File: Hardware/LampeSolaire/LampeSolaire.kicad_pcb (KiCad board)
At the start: 2 copper layers, 85 x 100 mm, 126 parts, among them K1 RELAIS_DPDT, P1 1V8, P2 3V5, P3 3V5, T1 SI2333, T2 FDN337, T3 FDN337, T4 FDN337, T5 FDN337, U1 MCP73832, U2 MCP121, U3 NCP114ASN330T1G, U4 3V3 to 5V, U5 RF_RECEIVER, U6 PIC16F1827, U7 MCP6001R, U8 74LV00, X1 ICSP, X13 STOCK, X14 STOCK, X15 STOCK, X17 STOCK_1, X18 SOLAR_CELL, X2 PHOTO_RESISTOR, X3 WATER_SENSOR, X4 WATER_SENSOR, X5 LAMP, X6 STOCK_1, X8 BUZZER

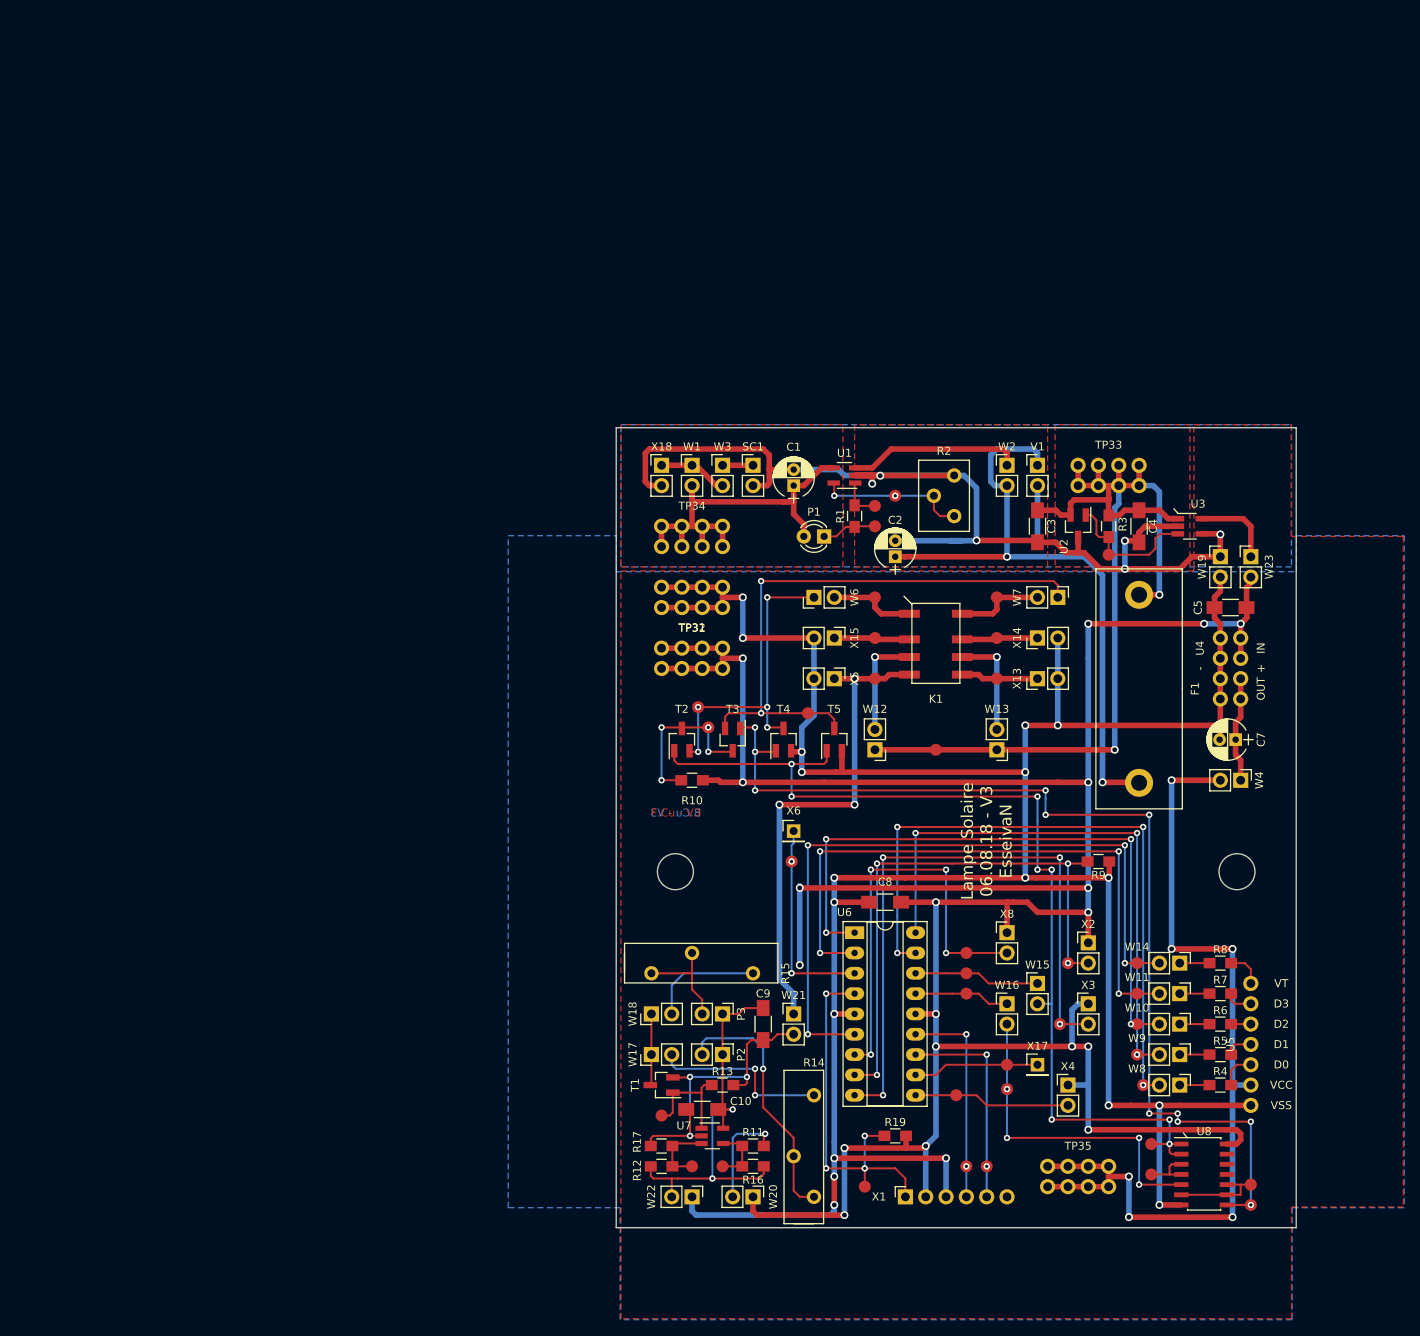
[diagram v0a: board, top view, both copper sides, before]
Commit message: Version 4
Nouveau PCB, modifications diverses au schéma
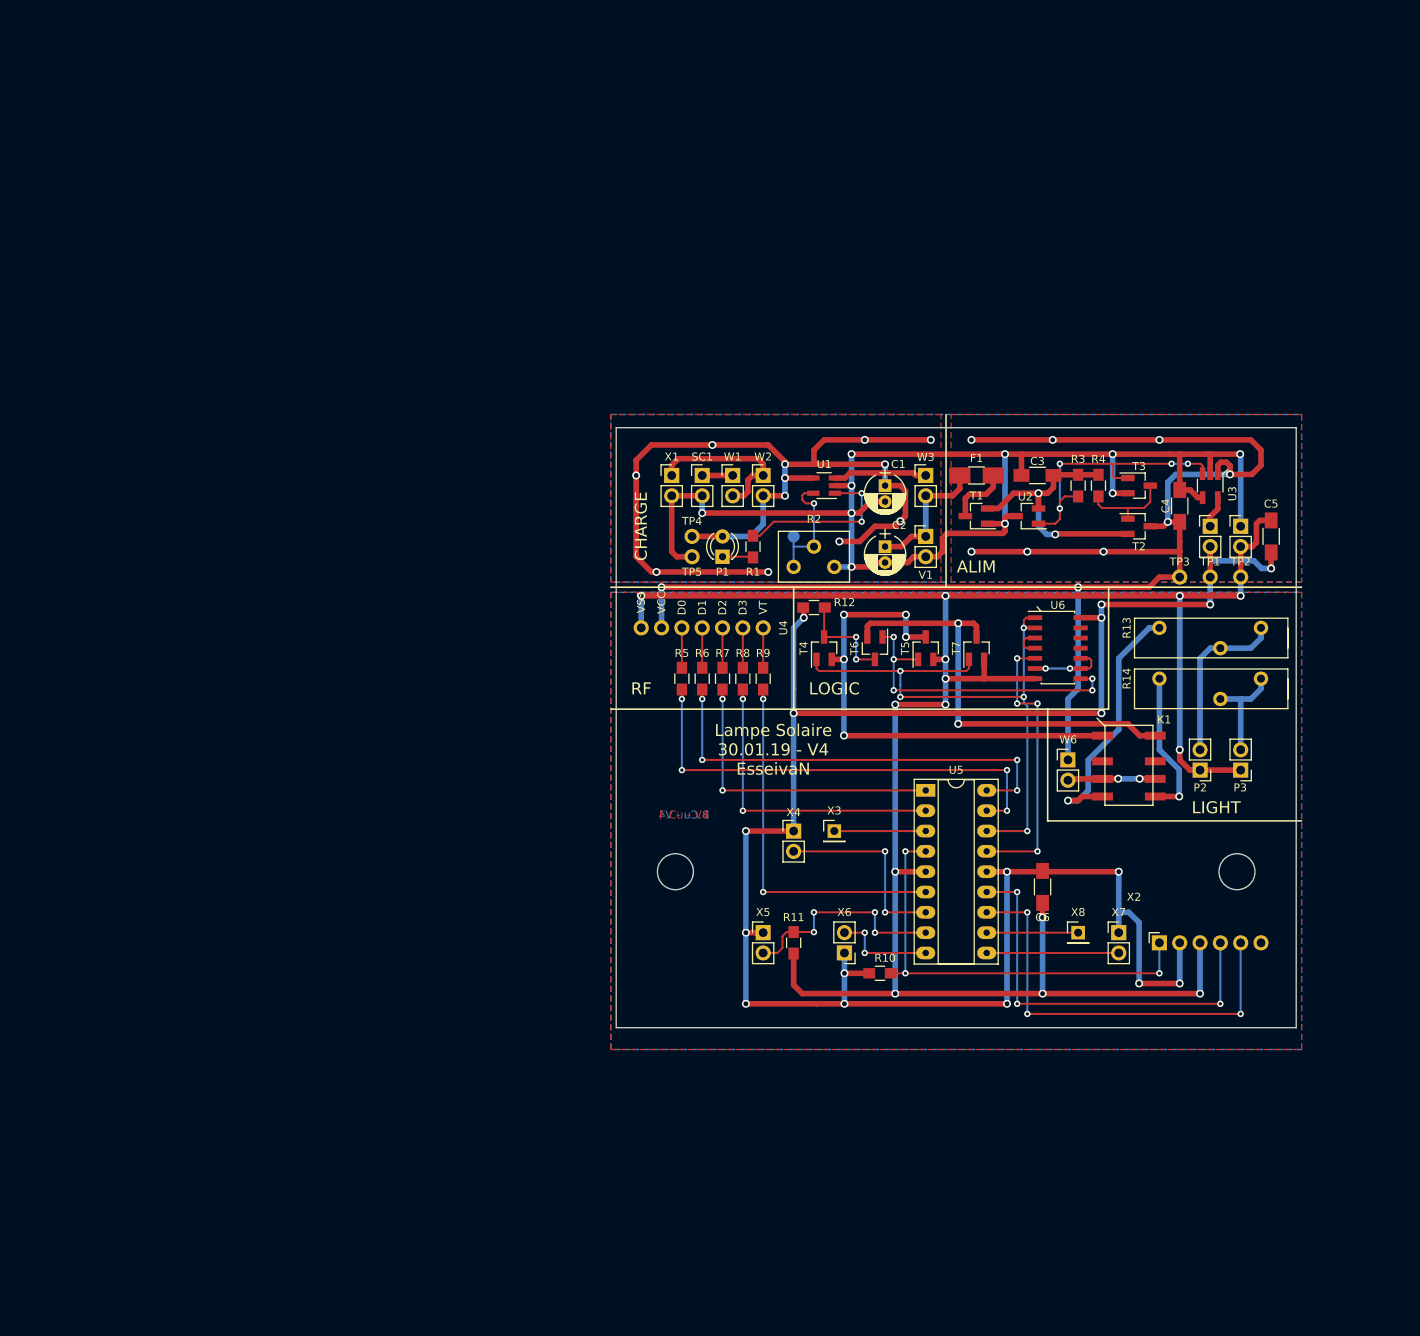
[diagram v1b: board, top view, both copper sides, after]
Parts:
- removed C10, C8, C9: 100nF, Capacitors_SMD:C_1206_HandSoldering
- removed C7: 4.7uF, MyLib:CP_Radial_D5.0mm_P2.00mm
- removed R15: 10, MyLib:Potentiometer_Trimmer_Bourns_3006P
- removed R16: 150k, MyLib:R_0805_HandSoldering
- removed R17: 100k, MyLib:R_0805_HandSoldering
- removed R19: 4k7, MyLib:R_0805_HandSoldering
- removed TP11, TP12, TP14, TP15, TP17, TP18, TP19, TP20, TP21, TP22, TP23, TP24, TP25, TP26, TP27, TP28, TP29, TP30, TP36, TP38, TP39, TP40, TP41, TP42, TP43, TP44, TP45, TP49, TP50, TP51, TP7, TP9: TestPoint, MyLib:Measurement_Point_Round-SMD-Pad_Small
- removed TP31, TP32, TP33, TP34, TP35: TestPoint_8, MyLib:Measurement_Point_Round-TH_Small_x8
- removed U7: MCP6001R, MyLib:SOT-23-5_HandSoldering
- removed U8: 74LV00, MyLib:SOIC-14
- removed W10, W11, W12, W13, W14, W15, W16, W17, W18, W19, W20, W21, W22, W23, W7, W8, W9: TEST_2P, MyLib:Pin_Header_Straight_1x02_Pitch2.54mm
- removed X13, X14, X15: STOCK, MyLib:Pin_Header_Straight_1x02_Pitch2.54mm
- removed X17: STOCK_1, MyLib:Pin_Header_Straight_1x01_Pitch2.54mm
- removed X18: SOLAR_CELL, MyLib:Pin_Header_Straight_1x02_Pitch2.54mm
- added C6: 100nF, Capacitors_SMD:C_1206_HandSoldering, F.Cu at (110.8, 101.9)
- added T6: FDN337, MyLib:SOT-23_Handsoldering, F.Cu at (89.8, 72.1)
- added T7: FDN337, MyLib:SOT-23_Handsoldering, F.Cu at (102.5, 72.1)
- added W5: TEST_2P, MyLib:Pin_Header_Straight_1x02_Pitch2.54mm, F.Cu at (131.8, 58.1)
- added X7: WATER_SENSOR, MyLib:Pin_Header_Straight_1x02_Pitch2.54mm, F.Cu at (120.3, 108.9)
- F1: footprint MyLib:FuseHolder_Schurter -> Fuse_Holders_and_Fuses:Fuse_SMD1206_HandSoldering
- R10: value 22 -> 4k7
- R11: value 110k -> 1M
- R12: value 100k -> 22
- R13: value 100k -> 10; footprint MyLib:R_0805_HandSoldering -> MyLib:Potentiometer_Trimmer_Bourns_3006P
- R4: value 4k7 -> 100k
- R5, R6, R7, R8: value 4k7 -> 1k
- R9: value 1M -> 4k7
- T2: value FDN337 -> SI2333
- TP1, TP2, TP3, TP4, TP5: value TestPoint -> TestPoint_8; footprint MyLib:Measurement_Point_Round-SMD-Pad_Small -> MyLib:Measurement_Point_Round-TH_Small
- TP6: moved to B.Cu
- U4: value 3V3 to 5V -> RF_RECEIVER; footprint MyLib:DC_DC -> MyLib:RF_RECEIVER
- U5: value RF_RECEIVER -> PIC16F1827; footprint MyLib:RF_RECEIVER -> MyLib:DIP-18
- U6: value PIC16F1827 -> 74xx00; footprint MyLib:DIP-18 -> MyLib:SOIC-14
- X1: value ICSP -> SOLAR_CELL; footprint MyLib:Pin_Header_Angled_1x06_Pitch2.54mm_reverse_invis -> MyLib:Pin_Header_Straight_1x02_Pitch2.54mm
- X2: value PHOTO_RESISTOR -> ICSP; footprint MyLib:Pin_Header_Straight_1x02_Pitch2.54mm -> MyLib:Pin_Header_Angled_1x06_Pitch2.54mm_reverse_invis
- X3: value WATER_SENSOR -> STOCK_1; footprint MyLib:Pin_Header_Straight_1x02_Pitch2.54mm -> MyLib:Pin_Header_Straight_1x01_Pitch2.54mm
- X4: value WATER_SENSOR -> BUZZER
- X5: value LAMP -> PHOTO_RESISTOR
- X6: value STOCK_1 -> WATER_SENSOR; footprint MyLib:Pin_Header_Straight_1x01_Pitch2.54mm -> MyLib:Pin_Header_Straight_1x02_Pitch2.54mm
- X8: value BUZZER -> STOCK_1; footprint MyLib:Pin_Header_Straight_1x02_Pitch2.54mm -> MyLib:Pin_Header_Straight_1x01_Pitch2.54mm
- moved X1 93.6 mm to (64.4, 51.7), turned to 0 degrees
- moved R5 82.1 mm to (65.7, 75.9), turned to 90 degrees
- moved T1 81.3 mm to (102.5, 55.5)
- moved R13 79.0 mm to (125.4, 69.5), turned to 180 degrees
- moved R6 77.8 mm to (68.2, 75.9), turned to 90 degrees
- moved R4 76.5 mm to (117.8, 51.7), turned to 90 degrees
- moved R7 73.6 mm to (70.8, 75.9), turned to 90 degrees
- moved P3 73.3 mm to (135.6, 86.0), turned to 180 degrees
- moved P2 71.2 mm to (130.5, 86.0), turned to 180 degrees
- moved R12 70.0 mm to (82.2, 67.0)
- moved R8 69.5 mm to (73.3, 75.9), turned to 90 degrees
- moved R14 67.6 mm to (125.4, 75.9), turned to 180 degrees
- moved U4 66.2 mm to (68.2, 69.5), turned to 0 degrees
- moved T2 63.1 mm to (122.9, 56.8), turned to 0 degrees
- moved T3 59.9 mm to (122.9, 51.7), turned to 0 degrees
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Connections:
- C3 pad 1: VBAT -> /VBAT_0
- F1 pad 1: VBAT -> Net-(F1-Pad1)
- K1 pad 4: LAMP -> Net-(K1-Pad4)
- K1 pad 6: Net-(K1-Pad6) -> Net-(K1-Pad3)
- P2 pad 1: Net-(C10-Pad2) -> GND
- P3 pad 1: Net-(C10-Pad2) -> GND
- R10 pad 1: Net-(R10-Pad1) -> /VPP
- R11 pad 1: /1V9 -> GND
- R12 pad 2: Net-(C10-Pad1) -> VCC
- R13 pad 1: Net-(R13-Pad1) -> Net-(K1-Pad4)
- R13 pad 2: Net-(C10-Pad1) -> Net-(P2-Pad2)
- R14 pad 1: Net-(R14-Pad1) -> Net-(K1-Pad5)
- R14 pad 2: Net-(P2-Pad2) -> Net-(P3-Pad2)
- R14 pad 3: Net-(P2-Pad2) -> Net-(P3-Pad2)
- R3 pad 2: VBAT -> /VBAT_0
- R4 pad 2: Net-(R4-Pad2) -> /VBAT_0
- R9 pad 1: GND -> /INT
- T1 pad 1: Net-(R13-Pad1) -> GND_ALIM
- T1 pad 2: Net-(C10-Pad1) -> /VBAT_0
- T1 pad 3: Net-(T1-Pad3) -> Net-(F1-Pad1)
- T2 pad 1: /SET -> Net-(R4-Pad1)
- T2 pad 2: Net-(T2-Pad2) -> /VBAT_0
- T2 pad 3: Net-(R10-Pad1) -> VBAT
- T3 pad 1: /RESET2 -> /~RST
- T3 pad 2: Net-(T3-Pad2) -> GND_ALIM
- T3 pad 3: Net-(R10-Pad1) -> Net-(R4-Pad1)
- T4 pad 1: /RESET2 -> /SET
- T4 pad 2: GND -> /+
- T4 pad 3: Net-(T2-Pad2) -> Net-(R12-Pad1)
- T5 pad 1: /SET -> /RESET2
- T5 pad 3: Net-(T3-Pad2) -> /+
- TP1 pad 1: Net-(P1-Pad1) -> VCC
- TP2 pad 1: /STAT -> GND
- TP3 pad 1: /VPROG -> VBAT
- TP4 pad 1: /~RST -> VSC
- TP5 pad 1: Net-(R10-Pad1) -> GND_ALIM
- TP6 pad 1: Net-(T2-Pad2) -> /VPROG
- U2 pad 2: VBAT -> /VBAT_0
- U4 pad 1: VCC -> GND
- U4 pad 2: GND -> VBAT
- U4 pad 3: GND -> Net-(R5-Pad2)
- U4 pad 4: Net-(C7-Pad1) -> Net-(R6-Pad2)
- U5 pad 1: GND -> Net-(R7-Pad1)
- U5 pad 2: +5V -> Net-(R8-Pad1)
- U5 pad 3: Net-(R4-Pad2) -> Net-(U5-Pad3)
- U5 pad 4: Net-(R5-Pad2) -> /VPP
- U5 pad 5: Net-(R6-Pad2) -> GND
- U5 pad 6: Net-(R7-Pad2) -> /INT
- U5 pad 7: Net-(R8-Pad2) -> Net-(U5-Pad7)
- U6 pad 1: Net-(TP14-Pad1) -> /SET
- U6 pad 10: Net-(TP20-Pad1) -> Net-(U6-Pad10)
- U6 pad 12: /ICSPCLK -> Net-(U6-Pad12)
- U6 pad 13: /ICSPDAT -> Net-(U6-Pad13)
- U6 pad 2: Net-(TP17-Pad1) -> /SET
- U6 pad 3: Net-(TP19-Pad1) -> Net-(U6-Pad3)
- U6 pad 4: /VPP -> Net-(U6-Pad3)
- U6 pad 5: GND -> /RESET
- U6 pad 6: /INT -> Net-(U6-Pad10)
- U6 pad 7: Net-(TP12-Pad1) -> GND
- U6 pad 8: Net-(R9-Pad2) -> /RESET2
- U6 pad 9: Net-(TP18-Pad1) -> Net-(U6-Pad10)
- W1 pad 1: Net-(W1-Pad1) -> Net-(SC1-Pad1)
- W1 pad 2: VSC -> Net-(W1-Pad2)
- W2 pad 1: Net-(U1-Pad3) -> Net-(W1-Pad2)
- W2 pad 2: Net-(C2-Pad1) -> VSC
- W3 pad 1: Net-(SC1-Pad1) -> Net-(U1-Pad3)
- W3 pad 2: Net-(W1-Pad1) -> Net-(C2-Pad1)
- W4 pad 1: Net-(C7-Pad1) -> GND_ALIM
- W4 pad 2: +5V -> GND
- W6 pad 1: Net-(T2-Pad2) -> VBAT
- W6 pad 2: /+ -> Net-(K1-Pad3)
- X1 pad 1: /VPP -> Net-(W1-Pad2)
- X1 pad 2: VCC -> GND_ALIM
- X2 pad 1: VCC -> /VPP
- X2 pad 2: Net-(R9-Pad2) -> VCC
- X3 pad 1: VCC -> Net-(U5-Pad3)
- X4 pad 2: Net-(TP20-Pad1) -> Net-(U5-Pad7)
- X5 pad 1: LAMP -> VCC
- X5 pad 2: GND -> Net-(R11-Pad2)
- X6 pad 1: Net-(TP19-Pad1) -> VCC
- X8 pad 1: VCC -> Net-(U5-Pad11)
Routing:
- net VCC: track 362.6 -> 248.8 mm, vias 19 -> 17
- net +5V: track 109.5 -> 0.00 mm, vias 6 -> 0
- net /RESET2: track 129.2 -> 38.9 mm, vias 11 -> 5
- net Net-(TP9-Pad1): track 83.3 -> 0.00 mm, vias 4 -> 0
- net Net-(TP14-Pad1): track 80.3 -> 0.00 mm, vias 4 -> 0
- net Net-(TP18-Pad1): track 79.8 -> 0.00 mm, vias 4 -> 0
- net Net-(TP17-Pad1): track 77.5 -> 0.00 mm, vias 4 -> 0
- net GND: track 344.2 -> 268.3 mm, vias 19 -> 14
- net Net-(T3-Pad2): track 72.1 -> 0.00 mm, vias 2 -> 0
- net VSC: track 49.9 -> 121.0 mm, vias 0 -> 12
- net Net-(TP11-Pad1): track 70.9 -> 0.00 mm, vias 3 -> 0
- net VBAT: track 123.6 -> 189.4 mm, vias 2 -> 10
- net Net-(R9-Pad2): track 70.6 -> 5.00 mm, vias 4 -> 0
- net Net-(C2-Pad1): track 79.7 -> 17.0 mm, vias 2 -> 0
- net LAMP: track 61.7 -> 0.00 mm, vias 3 -> 0
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- removed copper zone on F.Cu, net Net-(U1-Pad3)
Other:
- board size 85 x 100 mm -> 85 x 75 mm
- board text added: "B.Cu - V4"
- board text added: "B.Mask - V4"
- board text added: "BATTERY"
- board text added: "CHARGE"
- board text added: "F.Cu - V4"
- board text added: "F.Mask - V4"
- board text added: "LIGHT"
- board text added: "LOGIC"
- board text added: "Lampe Solaire 30.01.19 - V4 EsseivaN"
- board text added: "RF"
- board text removed: "B.Cu - V3"
- board text removed: "B.Mask - V3"
- board text removed: "DIGITAL"
- board text removed: "F.Cu - V3"
- board text removed: "F.Mask - V3"
- board text removed: "LAMP"
- board text removed: "Lampe Solaire 06.08.18 - V3 EsseivaN"

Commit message: Schematic v5 and PCB v5.1
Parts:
- removed R14: 10, MyLib:Potentiometer_Trimmer_Bourns_3006P
- removed TP1, TP2, TP3, TP4, TP5: TestPoint_8, MyLib:Measurement_Point_Round-TH_Small
- removed TP6: TestPoint, MyLib:Measurement_Point_Round-SMD-Pad_Small
- removed W1, W6: TEST_2P, MyLib:Pin_Header_Straight_1x02_Pitch2.54mm
- removed X3, X8: STOCK_1, MyLib:Pin_Header_Straight_1x01_Pitch2.54mm
- removed X5: PHOTO_RESISTOR, MyLib:Pin_Header_Straight_1x02_Pitch2.54mm
- removed X7: WATER_SENSOR, MyLib:Pin_Header_Straight_1x02_Pitch2.54mm
- added C7: 4.7uF, 0EsseivaN_Lib:CP_Radial_D5.0mm_P2.00mm, F.Cu at (115.2, 96.2)
- added C8: 100nF, Capacitors_SMD:C_1206_HandSoldering, B.Cu at (106.3, 67.0)
- added P4: 2V, 0EsseivaN_Lib:D_0603_HandSoldering, F.Cu at (82.2, 63.2)
- C1, C2: footprint MyLib:CP_Radial_D5.0mm_P2.00mm -> 0EsseivaN_Lib:CP_Radial_D5.0mm_P2.00mm
- C4, F1: moved to B.Cu
- K1: footprint MyLib:Relay -> 0EsseivaN_Lib:Relay
- P1: footprint MyLib:LED_D3.0mm -> 0EsseivaN_Lib:LED_D3.0mm
- P2, P3, SC1, X1, X4, X6: footprint MyLib:Pin_Header_Straight_1x02_Pitch2.54mm -> 0EsseivaN_Lib:CH_2P
- R1, R3, R4: footprint MyLib:R_0805_HandSoldering -> 0EsseivaN_Lib:R_0805_HandSoldering; moved to B.Cu
- R10, R12: footprint MyLib:R_0805_HandSoldering -> 0EsseivaN_Lib:R_0805_HandSoldering
- R11: value 1M -> 6; footprint MyLib:R_0805_HandSoldering -> Resistors_SMD:R_1206_HandSoldering; moved to B.Cu
- R13: value 10 -> 6; footprint MyLib:Potentiometer_Trimmer_Bourns_3006P -> Resistors_SMD:R_1206_HandSoldering; moved to B.Cu
- R2: value 100k -> 3k9; footprint MyLib:T93YB -> 0EsseivaN_Lib:R_0805_HandSoldering
- R5: value 1k -> 1K; footprint MyLib:R_0805_HandSoldering -> 0EsseivaN_Lib:R_0805_HandSoldering; moved to B.Cu
- R6: value 1k -> 330R; footprint MyLib:R_0805_HandSoldering -> 0EsseivaN_Lib:R_0805_HandSoldering; moved to B.Cu
- R7: value 1k -> 100k; footprint MyLib:R_0805_HandSoldering -> 0EsseivaN_Lib:R_0805_HandSoldering; moved to B.Cu
- R8: value 1k -> 1K; footprint MyLib:R_0805_HandSoldering -> 0EsseivaN_Lib:R_0805_HandSoldering
- R9: value 4k7 -> 1K; footprint MyLib:R_0805_HandSoldering -> 0EsseivaN_Lib:R_0805_HandSoldering
- T1, T6, T7: footprint MyLib:SOT-23_Handsoldering -> 0EsseivaN_Lib:SOT-23_Handsoldering
- T2, T3, T4, T5: footprint MyLib:SOT-23_Handsoldering -> 0EsseivaN_Lib:SOT-23_Handsoldering; moved to B.Cu
- U1: footprint MyLib:SOT-23-5_HandSoldering -> 0EsseivaN_Lib:SOT-23-5_HandSoldering
- U2: footprint ShockAccel:SOT-23_Handsoldering -> 0EsseivaN_Lib:SOT-23_Handsoldering; moved to B.Cu
- U3: footprint MyLib:TSOP-5 -> 0EsseivaN_Lib:TSOP-5; moved to B.Cu
- U4: value RF_RECEIVER -> MRF89XAM8A; footprint MyLib:RF_RECEIVER -> 0EsseivaN_Lib:MRF89XAM8A
- U5: footprint MyLib:DIP-18 -> Housings_SSOP:SSOP-20_5.3x7.2mm_Pitch0.65mm
- U6: footprint MyLib:SOIC-14 -> 0EsseivaN_Lib:SOIC-14
- V1: footprint MyLib:Pin_Header_Straight_1x02_Pitch2.54mm -> 0EsseivaN_Lib:CH_3P
- W2, W3, W4, W5: footprint MyLib:Pin_Header_Straight_1x02_Pitch2.54mm -> 0EsseivaN_Lib:Pin_Header_Straight_1x02_Pitch2.54mm
- X2: footprint MyLib:Pin_Header_Angled_1x06_Pitch2.54mm_reverse_invis -> 0EsseivaN_Lib:Pin_Header_Angled_1x06_Pitch2.54mm
- moved X2 70.0 mm to (60.6, 82.2), turned to 180 degrees
- moved U6 61.3 mm to (65.7, 111.4), turned to 90 degrees
- moved U4 54.3 mm to (121.6, 79.7), turned to 180 degrees
- moved R5 52.2 mm to (117.8, 79.6), turned to 270 degrees
- moved R13 50.9 mm to (100.5, 114.0)
- moved P2 46.4 mm to (91.6, 111.4), turned to 0 degrees
- moved X6 43.9 mm to (102.5, 68.2)
- moved T7 43.8 mm to (81.0, 110.2), turned to 180 degrees
- moved T5 43.7 mm to (77.1, 111.4), turned to 0 degrees
- moved P3 43.3 mm to (100.5, 111.4), turned to 0 degrees
- moved T6 42.8 mm to (81.0, 114.0), turned to 0 degrees
- moved T4 40.7 mm to (82.2, 112.7)
- moved R12 39.5 mm to (78.5, 106.3)
- moved R10 38.9 mm to (72.1, 78.4), turned to 270 degrees
- moved K1 36.7 mm to (86.0, 96.2)
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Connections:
- K1 pad 2: Net-(K1-Pad2) -> (no net)
- K1 pad 3: Net-(K1-Pad3) -> VBAT
- K1 pad 6: Net-(K1-Pad3) -> VBAT
- K1 pad 7: Net-(K1-Pad7) -> (no net)
- P1 pad 1: Net-(P1-Pad1) -> VSC
- P1 pad 2: VSC -> Net-(P1-Pad2)
- P2 pad 1: GND -> Net-(P2-Pad1)
- P2 pad 2: Net-(P2-Pad2) -> GND
- P3 pad 1: GND -> Net-(P3-Pad1)
- P3 pad 2: Net-(P3-Pad2) -> GND
- R1 pad 2: Net-(P1-Pad1) -> Net-(P1-Pad2)
- R11 pad 1: GND -> Net-(P2-Pad1)
- R11 pad 2: Net-(R11-Pad2) -> Net-(K1-Pad4)
- R13 pad 1: Net-(K1-Pad4) -> Net-(P3-Pad1)
- R13 pad 2: Net-(P2-Pad2) -> Net-(K1-Pad5)
- R2 pad 1: /VPROG -> GND_ALIM
- R5 pad 1: Net-(R5-Pad1) -> /RESET_RF
- R5 pad 2: Net-(R5-Pad2) -> VCC
- R6 pad 1: Net-(R6-Pad1) -> Net-(P4-Pad1)
- R6 pad 2: Net-(R6-Pad2) -> VCC
- R7 pad 1: Net-(R7-Pad1) -> /WATER
- R7 pad 2: Net-(R7-Pad2) -> GND
- R8 pad 1: Net-(R8-Pad1) -> /~CSDATA
- R8 pad 2: Net-(R8-Pad2) -> VCC
- R9 pad 1: /INT -> /~CSCON
- R9 pad 2: Net-(R9-Pad2) -> VCC
- U4 pad 2: VBAT -> /RESET_RF
- U4 pad 3: Net-(R5-Pad2) -> /~CSCON
- U4 pad 4: Net-(R6-Pad2) -> /IRQ0
- U4 pad 5: Net-(R7-Pad2) -> /MOSI
- U4 pad 6: Net-(R8-Pad2) -> /SCK
- U4 pad 7: Net-(R9-Pad2) -> /MISO
- U5 pad 1: Net-(R7-Pad1) -> /~CSCON
- U5 pad 10: Net-(U5-Pad10) -> /SCK
- U5 pad 11: Net-(U5-Pad11) -> /IRQ1
- U5 pad 17: Net-(R5-Pad1) -> /RESET_RF
- U5 pad 18: Net-(R6-Pad1) -> /~CSDATA
- U5 pad 2: Net-(R8-Pad1) -> /LED
- U5 pad 3: Net-(U5-Pad3) -> /BUZZER
- U5 pad 6: /INT -> /IRQ0
- U5 pad 7: Net-(U5-Pad7) -> /MISO
- U5 pad 8: Net-(R11-Pad2) -> /MOSI
- U5 pad 9: Net-(U5-Pad9) -> /WATER
- U6 pad 11: Net-(U6-Pad11) -> (no net)
- U6 pad 12: Net-(U6-Pad12) -> (no net)
- U6 pad 13: Net-(U6-Pad13) -> (no net)
- W2 pad 1: Net-(W1-Pad2) -> Net-(SC1-Pad1)
- X1 pad 1: Net-(W1-Pad2) -> Net-(SC1-Pad1)
- X4 pad 2: Net-(U5-Pad7) -> /BUZZER
- X6 pad 2: Net-(U5-Pad9) -> /WATER
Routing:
- net VBAT: track 189.4 -> 93.2 mm, vias 10 -> 4
- net VSC: track 121.0 -> 35.2 mm, vias 12 -> 3
- net /IRQ0: track 0.00 -> 74.1 mm, vias 0 -> 6
- net /SCK: track 0.00 -> 71.4 mm, vias 0 -> 8
- net /WATER: track 0.00 -> 66.6 mm, vias 0 -> 5
- net /MOSI: track 0.00 -> 65.3 mm, vias 0 -> 6
- net /~CSCON: track 0.00 -> 61.9 mm, vias 0 -> 7
- net Net-(R5-Pad1): track 58.3 -> 0.00 mm, vias 4 -> 0
- net Net-(R6-Pad1): track 55.8 -> 0.00 mm, vias 4 -> 0
- net /MISO: track 0.00 -> 51.4 mm, vias 0 -> 2
- net /INT: track 45.6 -> 0.00 mm, vias 2 -> 0
- net GND_ALIM: track 170.8 -> 125.5 mm, vias 10 -> 8
- net /RESET_RF: track 0.00 -> 44.4 mm, vias 0 -> 2
- net /~CSDATA: track 0.00 -> 40.5 mm, vias 0 -> 4
- net /IRQ1: track 0.00 -> 38.1 mm, vias 0 -> 6
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- removed copper zone on B.Cu, net GND
- removed copper zone on B.Cu, net GND_ALIM
- removed copper zone on F.Cu, net VBAT
- removed copper zone on F.Cu, net VCC
- removed copper zone on F.Cu, net VSC
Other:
- net class alim_mcu added: clearance 0.15, trace_width 0.45, via_dia 0.8, via_drill 0.4
